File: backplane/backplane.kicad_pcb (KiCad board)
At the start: 2 copper layers, 150 x 150 mm, 9 parts

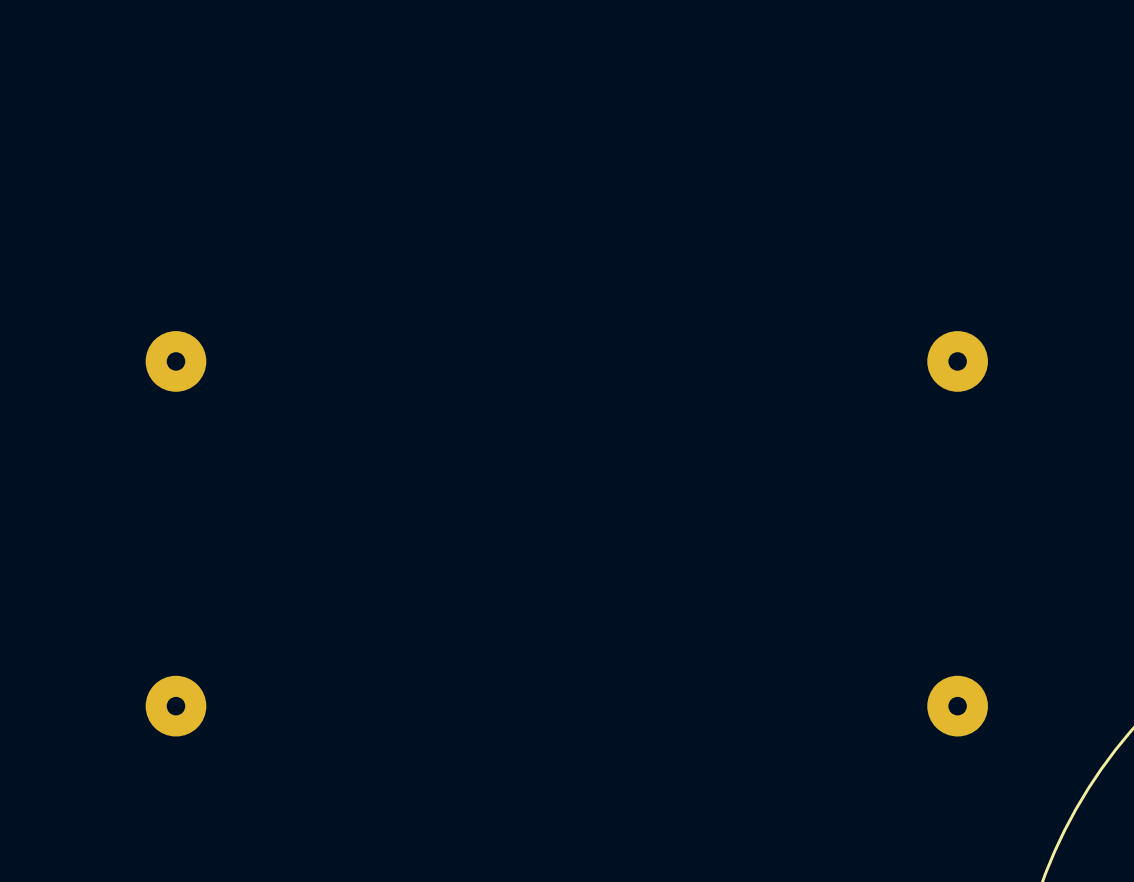
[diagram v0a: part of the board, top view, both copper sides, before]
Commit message: Updated footprint for Atheros wifi module (wf-np9202)
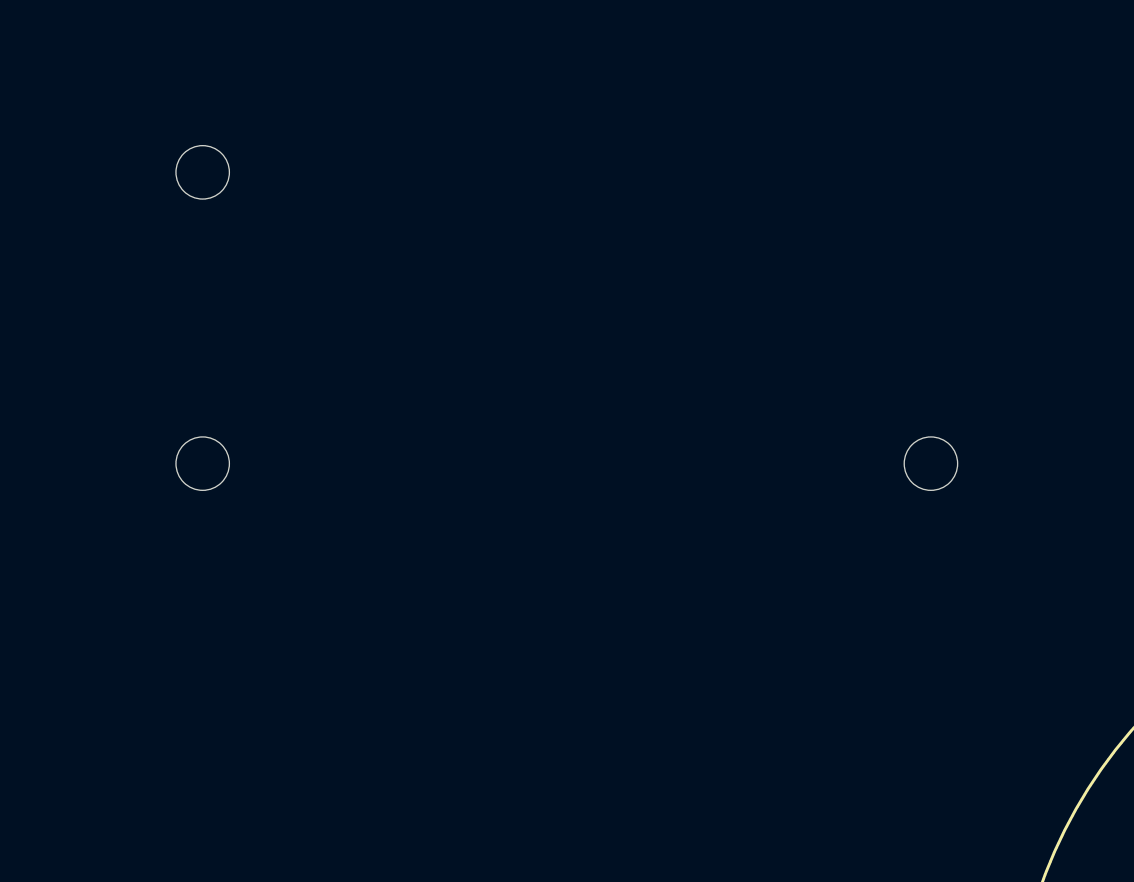
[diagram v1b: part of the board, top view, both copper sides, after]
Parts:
- moved Atheros WiFi Module 8.89 mm to (41.9, 83.8)
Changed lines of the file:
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@@
     (uvia_drill 0.1)
+  )
+  (module DxWiFi:Atheros (layer F.Cu)
+    (at 41.91 83.82)
+    (fp_text reference "Atheros WiFi Module" (at 17.5 -3.5) (layer F.Fab) hide
+      (effects (font (size 1 1) (thickness 0.15)))
+    )
+    (fp_text value "Atheros WiFi Module" (at 17.5 -1.27) (layer B.SilkS)
+      (effects (font (size 1 1) (thickness 0.15)))
+    )
+    (fp_text user USB (at 39.37 -13) (layer B.SilkS)
+      (effects (font (size 1 1) (thickness 0.15)))
+    )
+    (fp_line (start 36 -7.03) (end 35 -7.03) (layer B.SilkS) (width 0.12))
+    (fp_line (start 36 -7.03) (end 36 -15.03) (layer B.SilkS) (width 0.12))
+    (fp_line (start 35 -15.03) (end 36 -15.03) (layer B.SilkS) (width 0.12))
+    (fp_line (start 0 -17) (end 0 0) (layer B.SilkS) (width 0.12))
+    (fp_line (start 35 -17) (end 0 -17) (layer B.SilkS) (width 0.12))
+    (fp_line (start 35 0) (end 35 -17) (layer B.SilkS) (width 0.12))
+    (fp_line (start 0 0) (end 35 0) (layer B.SilkS) (width 0.12))
+    (pad "" np_thru_hole circle (at 32.5 -2.5 180) (size 2.2 2.2) (drill 2.2) (layers *.Cu *.Mask))
+    (pad "" np_thru_hole circle (at 2.5 -14.5) (size 2.2 2.2) (drill 2.2) (layers *.Cu *.Mask))
+    (pad "" np_thru_hole circle (at 2.5 -2.5) (size 2.2 2.2) (drill 2.2) (layers *.Cu *.Mask))
   )
   (module DxWiFi:Raspberry-Pi-Zero (layer F.Cu)
@@
       (effects (font (size 1 1) (thickness 0.15)))
     )
+    (fp_line (start -1 -20.54) (end -1 -28.09) (layer B.SilkS) (width 0.12))
+    (fp_line (start -1 -28.09) (end 0 -28.09) (layer B.SilkS) (width 0.12))
+    (fp_line (start 0 -20.54) (end -1 -20.54) (layer B.SilkS) (width 0.12))
     (fp_line (start 0 0) (end 30 0) (layer B.SilkS) (width 0.12))
     (fp_line (start 30 0) (end 30 -65) (layer B.SilkS) (width 0.12))
@@
       (effects (font (size 1 1) (thickness 0.15)))
     )
-    (fp_line (start -1 -18.43) (end 0 -18.43) (layer B.SilkS) (width 0.12))
-    (fp_line (start -1 -16.43) (end -1 -18.43) (layer B.SilkS) (width 0.12))
-    (fp_line (start 0 -16.43) (end -1 -16.43) (layer B.SilkS) (width 0.12))
     (fp_line (start 30 -65) (end 0 -65) (layer B.SilkS) (width 0.12))
     (fp_line (start 0 -65) (end 0 0) (layer B.SilkS) (width 0.12))
     (fp_line (start 0 -7.54) (end -1 -7.54) (layer B.SilkS) (width 0.12))
-    (fp_line (start -1 -7.54) (end -1 -9.54) (layer B.SilkS) (width 0.12))
-    (fp_line (start -1 -9.54) (end 0 -9.54) (layer B.SilkS) (width 0.12))
+    (fp_line (start -1 -7.54) (end -1 -15.09) (layer B.SilkS) (width 0.12))
+    (fp_line (start -1 -15.09) (end 0 -15.09) (layer B.SilkS) (width 0.12))
     (pad "" np_thru_hole circle (at 3.5 -3.5) (size 2.75 2.75) (drill 2.75) (layers *.Cu *.Mask))
     (pad "" np_thru_hole circle (at 26.5 -61.5) (size 2.75 2.75) (drill 2.75) (layers *.Cu *.Mask))
@@
     (fp_curve (pts (xy -0.074989 0.165537) (xy -0.303201 0.254522) (xy -0.474286 -0.106178) (xy -0.682656 0.151478)) (layer B.SilkS) (width 0.2))
   )
-  (module DxWiFi:Atheros (layer F.Cu)
-    (at 41.91 92.71)
-    (fp_text reference "Atheros WiFi Module" (at 17.5 -3.5) (layer F.Fab) hide
-      (effects (font (size 1 1) (thickness 0.15)))
-    )
-    (fp_text value "Atheros WiFi Module" (at 17.5 -1.27) (layer B.SilkS)
-      (effects (font (size 1 1) (thickness 0.15)))
-    )
-    (fp_text user USB (at 39.37 -13) (layer B.SilkS)
-      (effects (font (size 1 1) (thickness 0.15)))
-    )
-    (fp_line (start 36 -12) (end 35 -12) (layer B.SilkS) (width 0.12))
-    (fp_line (start 36 -12) (end 36 -14) (layer B.SilkS) (width 0.12))
-    (fp_line (start 35 -14) (end 36 -14) (layer B.SilkS) (width 0.12))
-    (fp_line (start 0 -17) (end 0 0) (layer B.SilkS) (width 0.12))
-    (fp_line (start 35 -17) (end 0 -17) (layer B.SilkS) (width 0.12))
-    (fp_line (start 35 0) (end 35 -17) (layer B.SilkS) (width 0.12))
-    (fp_line (start 0 0) (end 35 0) (layer B.SilkS) (width 0.12))
-    (pad 4 thru_hole circle (at 1.4 -15.6) (size 2.5 2.5) (drill 0.762) (layers *.Cu *.Mask))
-    (pad 3 thru_hole circle (at 33.6 -15.6) (size 2.5 2.5) (drill 0.762) (layers *.Cu *.Mask))
-    (pad 2 thru_hole circle (at 33.6 -1.4) (size 2.5 2.5) (drill 0.762) (layers *.Cu *.Mask))
-    (pad 1 thru_hole circle (at 1.4 -1.4) (size 2.5 2.5) (drill 0.762) (layers *.Cu *.Mask))
-  )
   (module DxWiFi:Antenna (layer F.Cu)

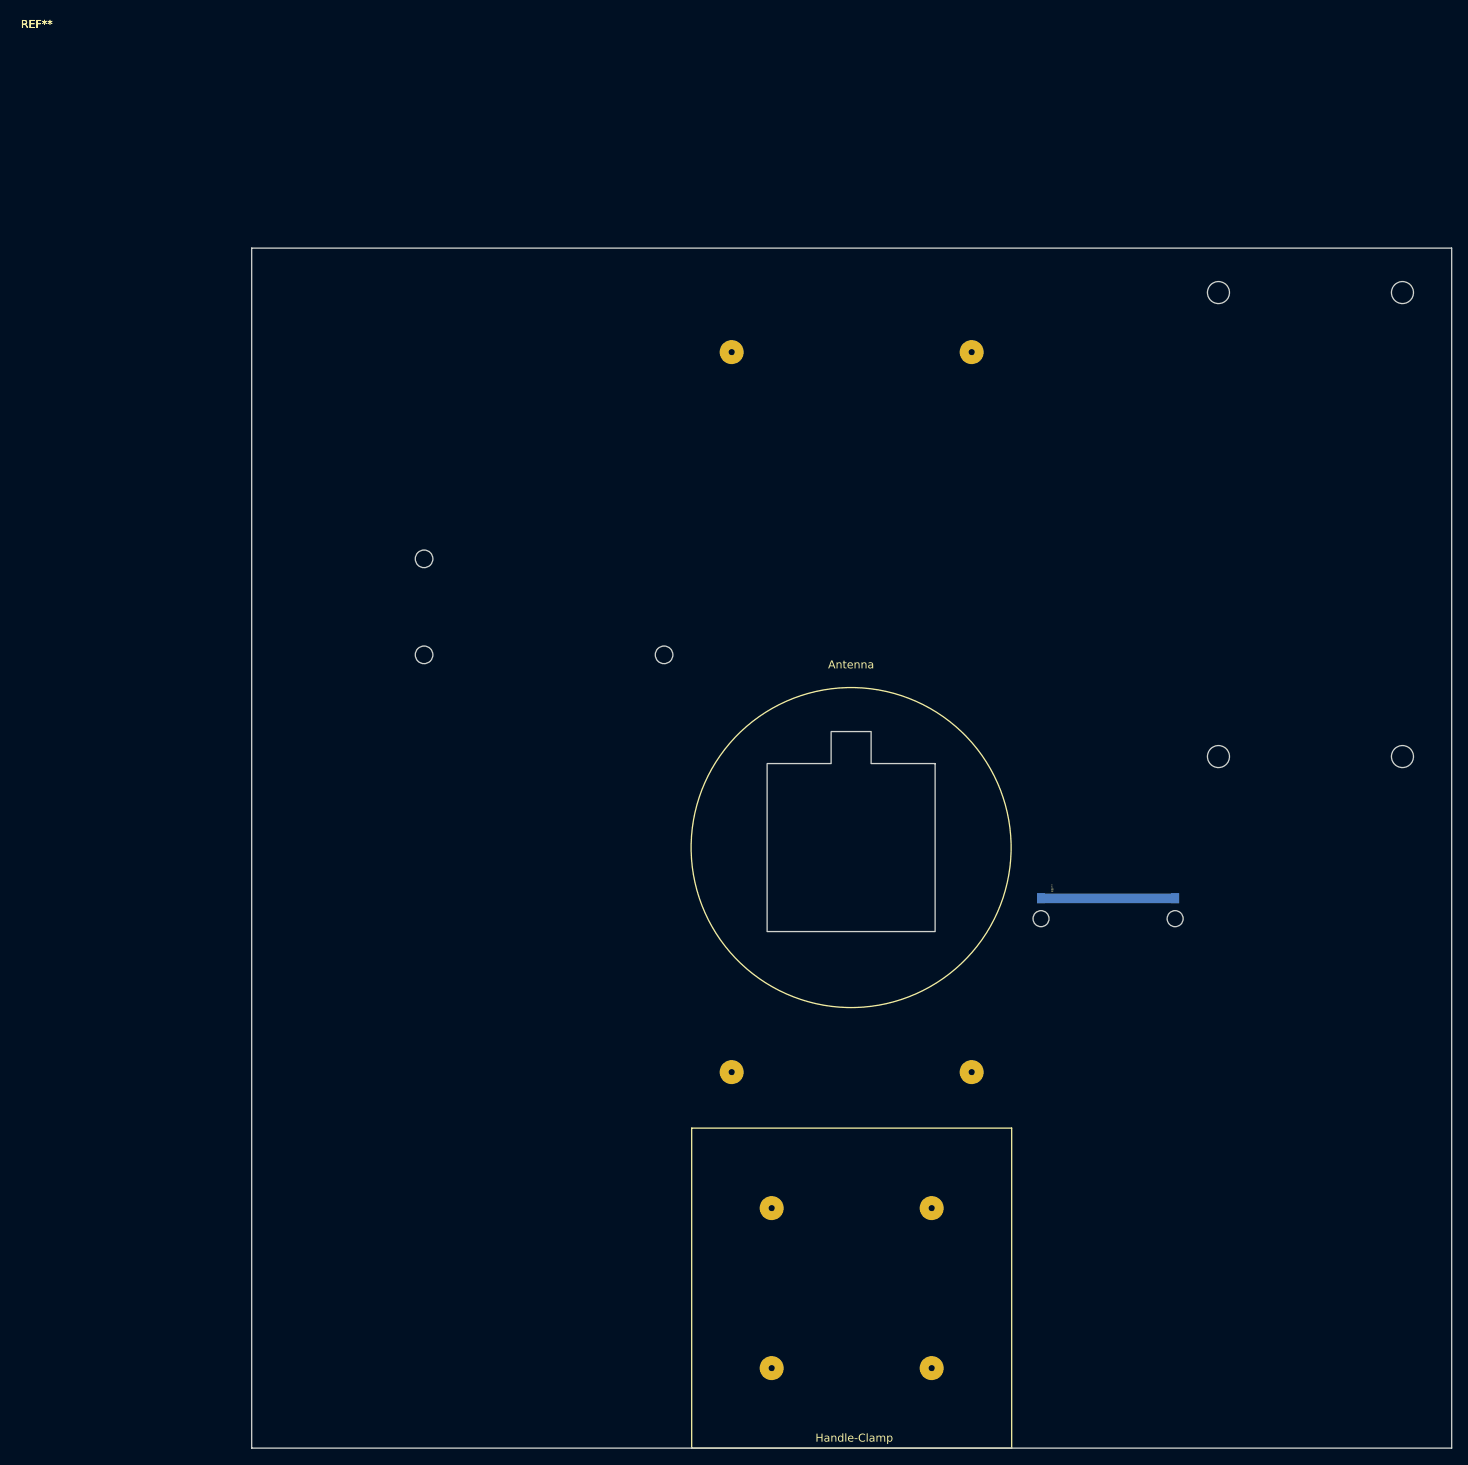
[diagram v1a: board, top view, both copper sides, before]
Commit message: Added holes for strings and modified microstrip
Board layout now reflects what users see when using the product from the
back of the board.  The side of the microstrip where the antenna will feed
in now has a rectangular hole.
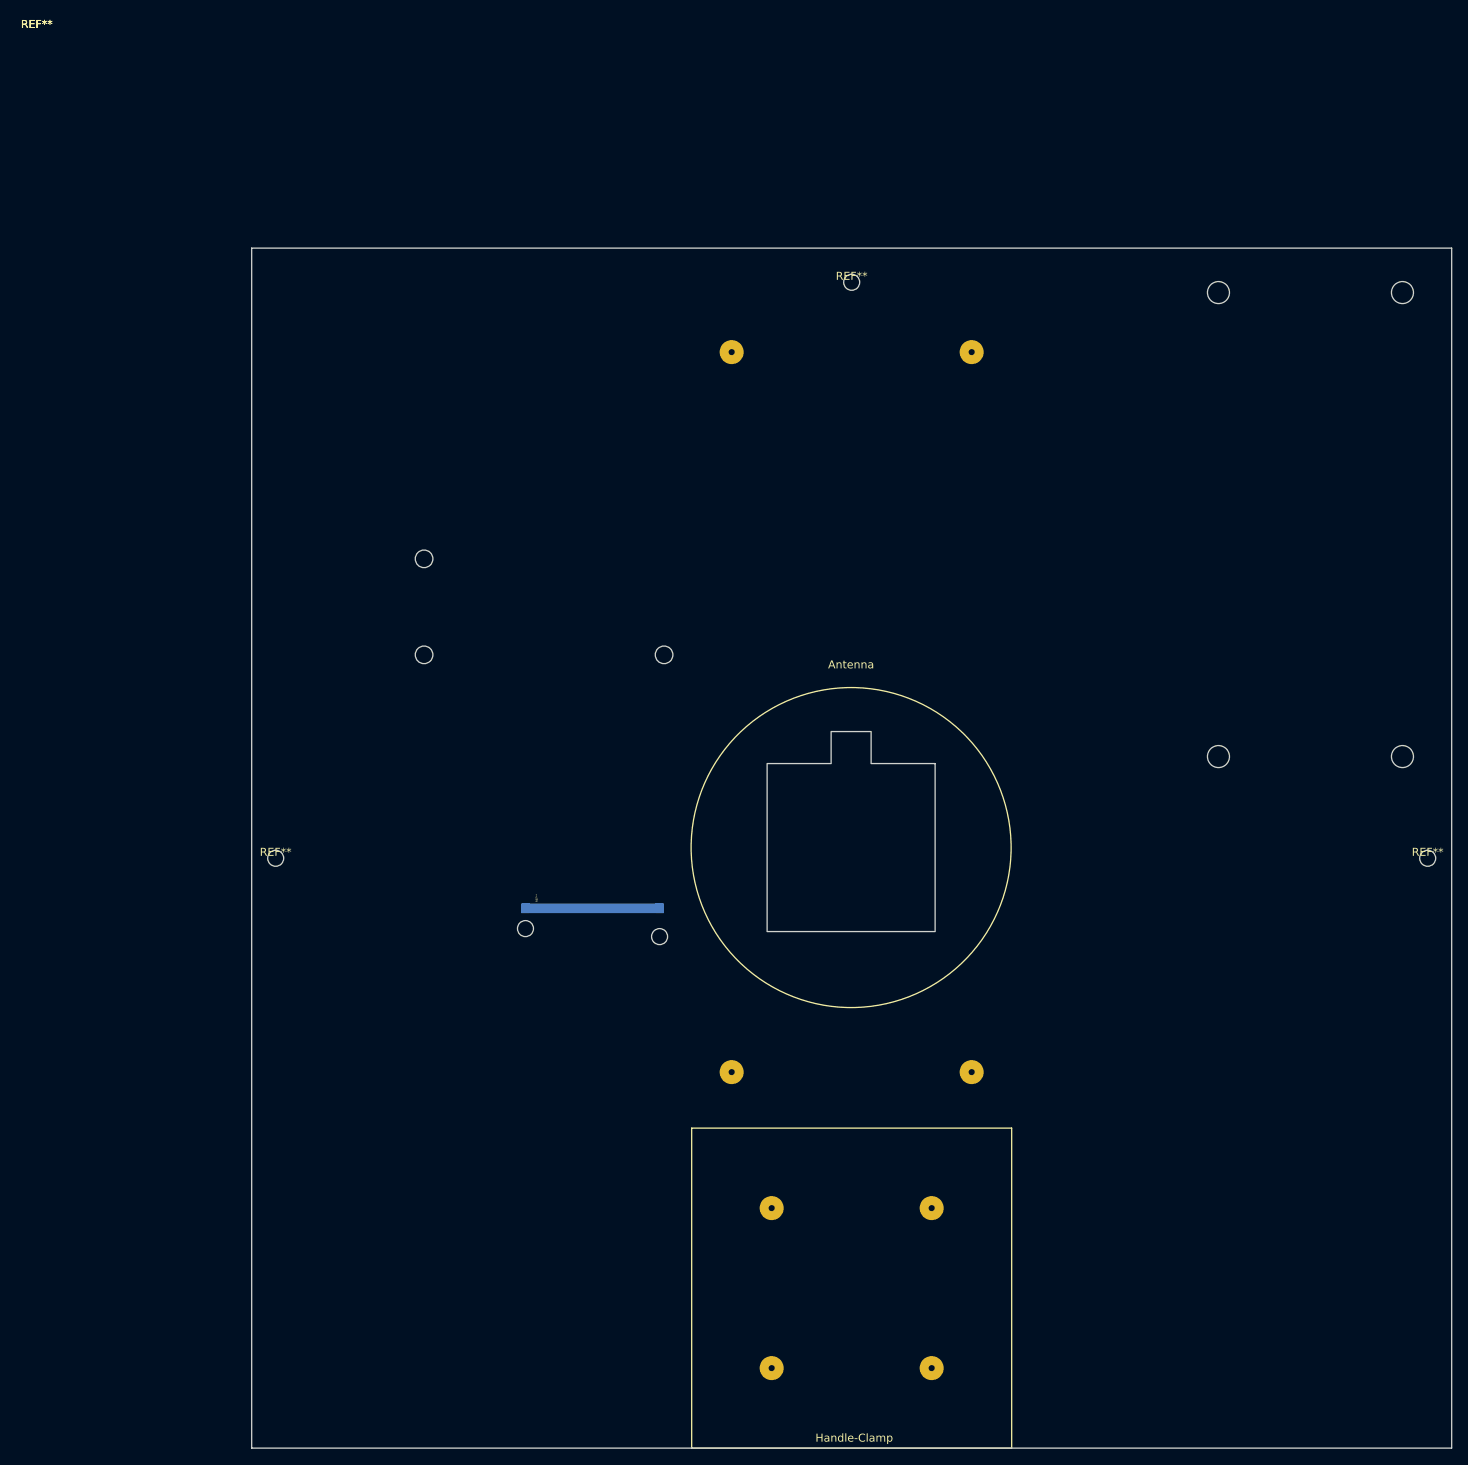
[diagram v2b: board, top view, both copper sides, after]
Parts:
- added REF**: string_mount, DxWiFi:string_mount, F.Cu at (25.9, 105.5)
- added REF**: string_mount, DxWiFi:string_mount, F.Cu at (97.9, 33.5)
- added REF**: string_mount, DxWiFi:string_mount, F.Cu at (169.9, 105.5)
- moved REF** 64.5 mm to (59.0, 113.0)
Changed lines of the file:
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@@
     (tracks 0)
     (zones 0)
-    (modules 9)
+    (modules 12)
     (nets 1)
   )
@@
     (mod_text_size 1 1)
     (mod_text_width 0.15)
-    (pad_size 0.25 0.25)
-    (pad_drill 0)
+    (pad_size 4 2)
+    (pad_drill 2)
     (pad_to_mask_clearance 0.051)
     (solder_mask_min_width 0.25)
@@
     (uvia_dia 0.3)
     (uvia_drill 0.1)
+  )
+  (module DxWiFi:string_mount (layer F.Cu)
+    (at 25.86 105.48)
+    (fp_text reference REF** (at 0 0.5) (layer F.SilkS)
+      (effects (font (size 1 1) (thickness 0.15)))
+    )
+    (fp_text value string_mount (at 0 -0.5) (layer F.Fab)
+      (effects (font (size 1 1) (thickness 0.15)))
+    )
+    (pad "" np_thru_hole circle (at 0 1.27) (size 2 2) (drill 2) (layers *.Cu *.Mask))
+  )
+  (module DxWiFi:string_mount (layer F.Cu)
+    (at 97.86 33.48)
+    (fp_text reference REF** (at 0 0.5) (layer F.SilkS)
+      (effects (font (size 1 1) (thickness 0.15)))
+    )
+    (fp_text value string_mount (at 0 -0.5) (layer F.Fab)
+      (effects (font (size 1 1) (thickness 0.15)))
+    )
+    (pad "" np_thru_hole circle (at 0 1.27) (size 2 2) (drill 2) (layers *.Cu *.Mask))
+  )
+  (module DxWiFi:string_mount (layer F.Cu)
+    (at 169.86 105.48)
+    (fp_text reference REF** (at 0 0.5) (layer F.SilkS)
+      (effects (font (size 1 1) (thickness 0.15)))
+    )
+    (fp_text value string_mount (at 0 -0.5) (layer F.Fab)
+      (effects (font (size 1 1) (thickness 0.15)))
+    )
+    (pad "" np_thru_hole circle (at 0 1.27) (size 2 2) (drill 2) (layers *.Cu *.Mask))
+  )
+  (module muwave_stub (layer F.Cu)
+    (at 59 113 270)
+    (fp_text reference REF** (at -1.27 0.5 270) (layer F.SilkS)
+      (effects (font (size 0.25 0.25) (thickness 0.05)))
+    )
+    (fp_text value muwave_stub (at 0 -0.5 270) (layer F.Fab)
+      (effects (font (size 0.25 0.25) (thickness 0.05)))
+    )
+    (pad 1 smd rect (at 0 -6.46615 270) (size 1.20938 17.7623) (layers B.Cu)
+      (clearance 12.6))
+    (pad 1 smd rect (at 0 0 270) (size 0.25 0.25) (layers B.Cu))
+    (pad 2 smd rect (at 0 -14.8473 270) (size 1.20938 1) (layers B.Cu B.Mask))
+    (pad 2 smd rect (at 0 1.915 270) (size 1.20938 1) (layers B.Cu B.Mask))
+    (pad "" np_thru_hole roundrect (at 3.54 -14.8473 270) (size 4 2) (drill 2) (layers *.Cu) (roundrect_rratio 0.25)
+      (clearance 0.5))
+    (pad "" np_thru_hole circle (at 2.54 1.915 270) (size 2 2) (drill 2) (layers *.Cu *.Mask))
   )
   (module DxWiFi:Atheros (layer F.Cu)
@@
     )
   )
-  (module muwave_stub (layer F.Cu)
-    (at 123.444 111.76 270)
-    (fp_text reference REF** (at -1.27 0.5 270) (layer F.SilkS)
-      (effects (font (size 0.25 0.25) (thickness 0.05)))
-    )
-    (fp_text value muwave_stub (at 0 -0.5 270) (layer F.Fab)
-      (effects (font (size 0.25 0.25) (thickness 0.05)))
-    )
-    (pad 1 smd rect (at 0 -6.46615 270) (size 1.20938 17.7623) (layers B.Cu)
-      (clearance 12.6))
-    (pad 1 smd rect (at 0 0 270) (size 0.25 0.25) (layers B.Cu))
-    (pad 2 smd rect (at 0 -14.8473 270) (size 1.20938 1) (layers B.Cu B.Mask))
-    (pad 2 smd rect (at 0 1.915 270) (size 1.20938 1) (layers B.Cu B.Mask))
-    (pad "" np_thru_hole circle (at 2.54 -14.8473 270) (size 2 2) (drill 2) (layers *.Cu))
-    (pad "" np_thru_hole circle (at 2.54 1.915 270) (size 2 2) (drill 2) (layers *.Cu *.Mask))
-  )
   (gr_line (start 22.86 180.48) (end 22.86 30.48) (layer Edge.Cuts) (width 0.05))
